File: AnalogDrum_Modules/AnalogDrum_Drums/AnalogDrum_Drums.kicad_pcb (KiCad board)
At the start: 2 copper layers, 100.3 x 160 mm, 95 parts, among them J101 Conn_01x05_Male, Q401 2N3904, Q402 2N3904, Q403 2N3904, SW101 SW_SPDT, SW201 SW_DPDT_x2, SW202 SW_DPDT_x2, U201 TL074, U301 LM13700, U302 NE5532, U401 TL074, U402 LM358

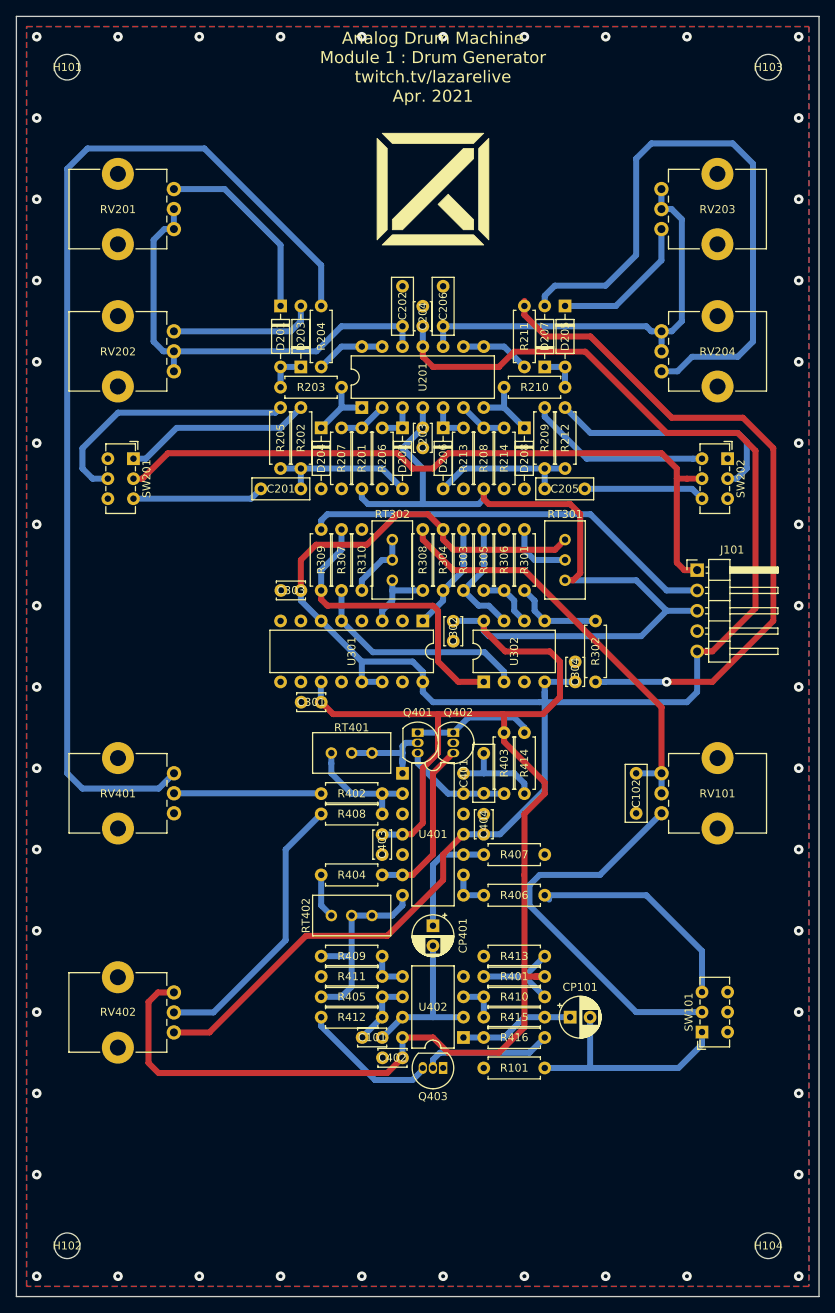
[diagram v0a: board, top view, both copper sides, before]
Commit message: Version 0.1.1
Corrections mineures :
- Vérification des potentiomètres
- Passage des connecteurs de carte e n JST
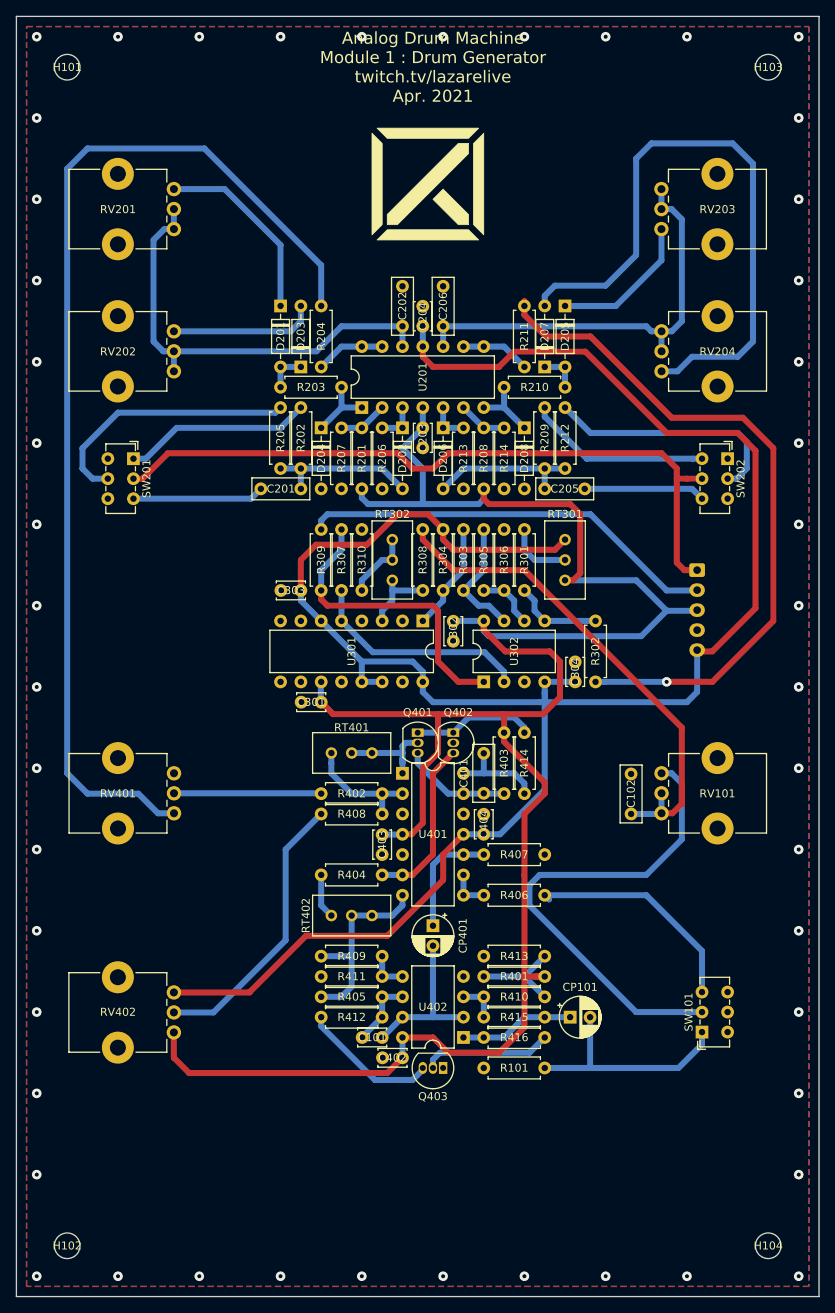
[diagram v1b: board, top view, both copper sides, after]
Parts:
- J101: footprint Connector_PinHeader_2.54mm:PinHeader_1x05_P2.54mm_Horizontal -> Connector_JST:JST_EH_B5B-EH-A_1x05_P2.50mm_Vertical; moved to B.Cu
- moved C102 5.12 mm to (118.7, 127.6), turned to 90 degrees
- moved REF** 0.90 mm to (93.3, 48.9)
- turned J101 to 270 degrees
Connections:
- RV101 pad 1: Net-(RV101-Pad1) -> /Mono_VCA/SIG_IN
- RV101 pad 3: /Mono_VCA/SIG_IN -> Net-(RV101-Pad3)
- RV401 pad 1: /Envelop_Generator/EGA_OUT -> GNDA
- RV401 pad 3: GNDA -> /Envelop_Generator/EGA_OUT
- RV402 pad 1: +12V -> -12V
- RV402 pad 3: -12V -> +12V
- SW101 pad 2: Net-(RV101-Pad1) -> Net-(RV101-Pad3)
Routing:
- net Net-(RV101-Pad3): track 0.00 -> 61.1 mm
- net Net-(RV101-Pad1): track 49.9 -> 0.00 mm
- net +12V: track 284.9 -> 273.9 mm
- net /Mono_VCA/SIG_IN: track 53.7 -> 62.3 mm
- net -12V: track 270.3 -> 268.2 mm
